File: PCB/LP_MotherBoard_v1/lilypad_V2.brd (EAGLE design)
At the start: 61 x 53.7 mm, 30 parts, among them U1 INA169QPWRQ1PW8-M, X4 BQ24074

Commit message: update board schematic
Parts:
- removed C1: 0.1µF, adafruit:C0805K
- removed R3: 10K, adafruit:M0805
- removed R5: 0.1/1%, resistor-shunt:SMT-REF
- removed U1: INA169QPWRQ1PW8-M, INA169-SOP8:PW8-M
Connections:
- removed net TMP_PRB: HP1.16, JP7.2, R12.2
- net A1: no longer R3.1, U1.6
- net CHARGER_IN: no longer R5.1, U1.2
- net GND: now also JP9.2; no longer C1.2, R3.2, R5.2, U1.1, U1.4
- net P11: now also JP7.2, R12.2
- net VCC: no longer C1.1, U1.8
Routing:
- net CHARGER_IN: track 19.6 -> 5.73 mm
- net TMP_PRB: track 7.71 -> 0.00 mm
- net A1: track 41.4 -> 34.7 mm
- net P11: track 0.00 -> 4.29 mm
- net VCC: track 3.58 -> 0.00 mm, vias 1 -> 0

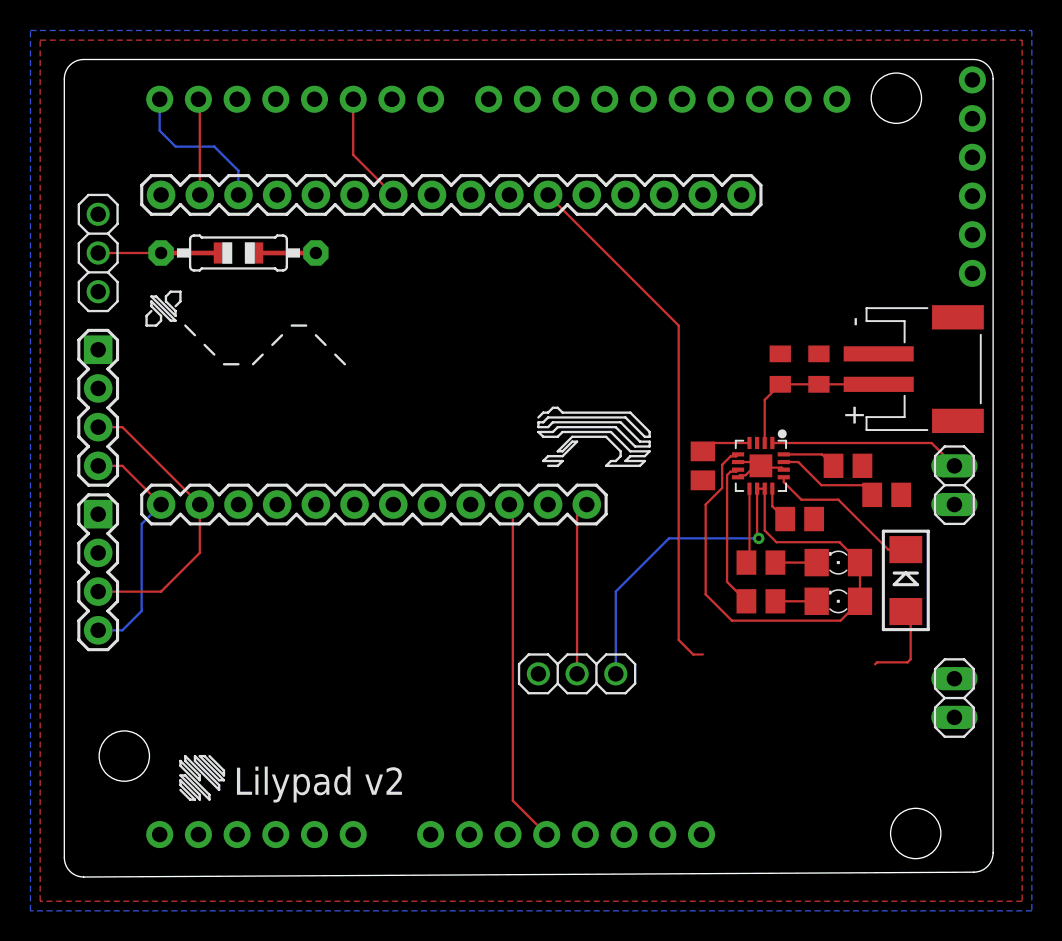
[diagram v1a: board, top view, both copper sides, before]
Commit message: Update PCB
Changed the wire connection type, adjusted for clearance. Fixed GND plane and moved the digital temp. sensor pin to 11.
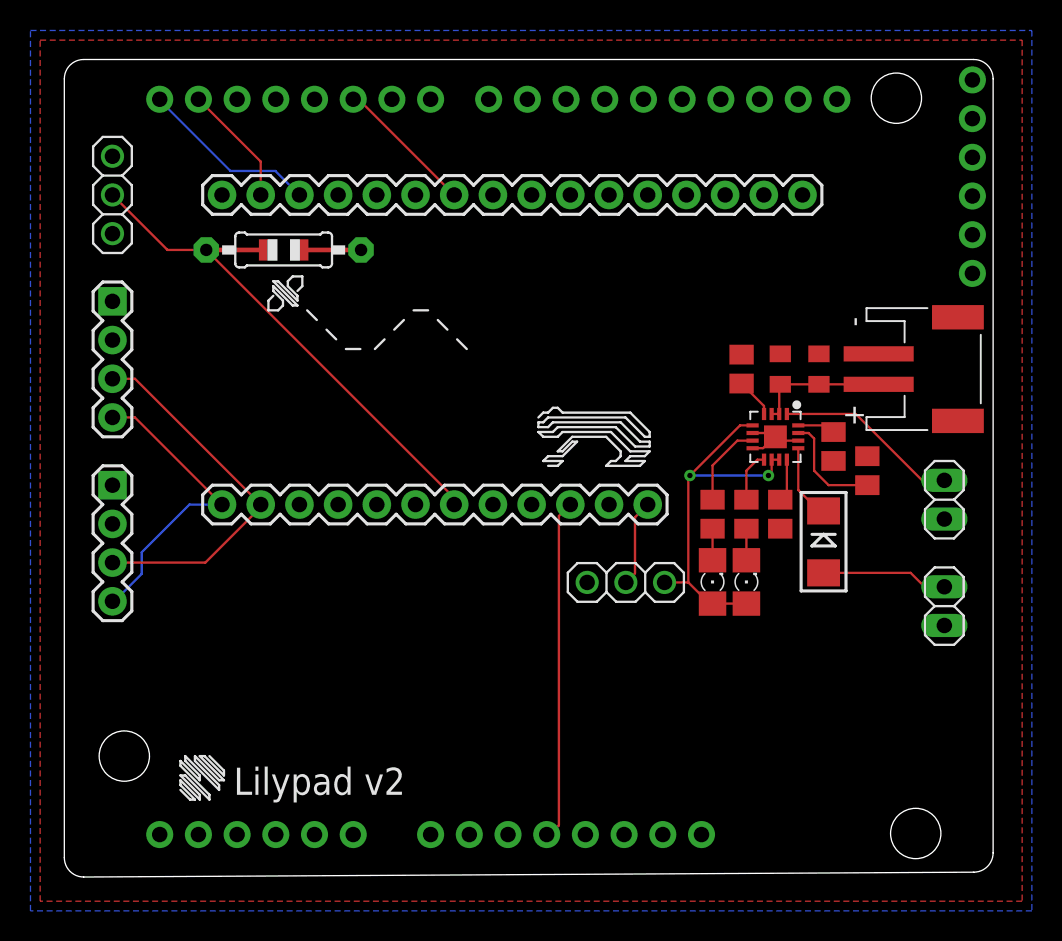
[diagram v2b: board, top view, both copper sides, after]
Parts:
- moved GREEN 8.35 mm to (45.1, 19.1), turned to 90 degrees
- moved R8 6.84 mm to (47.0, 33.0), turned to 90 degrees
- moved JP1 6.80 mm to (39.4, 19.0)
- moved R11 6.54 mm to (45.1, 23.5), turned to 270 degrees
- moved RED 6.16 mm to (47.3, 19.1), turned to 90 degrees
- moved JP9 6.07 mm to (60.3, 17.5)
- moved D2 5.97 mm to (52.4, 21.7)
- moved HP1 4.00 mm to (51.0, 44.5)
- moved HP2 4.00 mm to (40.8, 24.1)
- moved JP7 3.92 mm to (5.70, 44.5)
- moved R7 3.31 mm to (47.3, 23.5), turned to 270 degrees
- moved J1 3.31 mm to (5.70, 37.5)
- moved R12 2.97 mm to (16.9, 40.8)
- moved X4 2.13 mm to (49.2, 28.6)
- moved J2 2.12 mm to (5.70, 25.4)
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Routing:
- net A1: track 34.7 -> 0.00 mm
- net VBAT: track 54.1 -> 25.3 mm, vias 1 -> 2
- net P11: track 4.29 -> 31.1 mm
- net VIN: track 11.4 -> 5.71 mm
- net N$2: track 10.2 -> 4.97 mm
- net SCL: track 19.7 -> 24.6 mm
- net SDA: track 16.1 -> 20.2 mm
- net !PGOOD: track 9.68 -> 5.55 mm
- net CHARGER_IN: track 5.73 -> 8.31 mm
- net RX: track 9.91 -> 11.8 mm
- net 4GONOFF: track 7.37 -> 9.23 mm
- net VLIPO: track 10.7 -> 8.93 mm
- net TX: track 6.32 -> 7.97 mm
- net !CHG: track 4.93 -> 3.36 mm
- net ISET: track 3.58 -> 2.68 mm
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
